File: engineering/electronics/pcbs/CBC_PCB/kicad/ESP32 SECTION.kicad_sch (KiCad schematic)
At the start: 20 parts, among them U2 2.4GHz, U4 1kΩ

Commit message: electronics: integrate CBC PCB updates
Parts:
- removed U4: 1kΩ, EasyEDA_Lib:R0402, symbol EasyEDA_Lib:MCS0402MC1001FE000
- added R69: 39Ω, EasyEDA_Lib:R0603, symbol CBC_PCB:0603WAF390JT5E
- C1: symbol EasyEDA_Lib:HGC0402R5105K250NTEJ -> CBC_PCB:HGC0402R5105K250NTEJ
- C18: symbol EasyEDA_Lib:CL21A475KBQNNNE -> CBC_PCB:CL21A475KBQNNNE
- C19, C22, C24: symbol EasyEDA_Lib:GRM21BR61H106KE43L -> CBC_PCB:GRM21BR61H106KE43L
- C20, C21, C23: symbol EasyEDA_Lib:CC0402KRX7R7BB104 -> CBC_PCB:CC0402KRX7R7BB104
- D3: symbol EasyEDA_Lib:SS14_C7420316 -> CBC_PCB:SS14_C7420316
- D4: symbol EasyEDA_Lib:USBLC6-2SC6 -> CBC_PCB:USBLC6-2SC6
- LED1: symbol EasyEDA_Lib:0603 Green 509-620mcd -> CBC_PCB:0603 Green 509-620mcd
- Q1: symbol EasyEDA_Lib:UMH3N -> CBC_PCB:UMH3N
- R7: symbol EasyEDA_Lib:RT0402BRD0710KL -> CBC_PCB:RT0402BRD0710KL
- R8, R9: symbol EasyEDA_Lib:0402WGF5101TCE -> CBC_PCB:0402WGF5101TCE
- SW1: symbol EasyEDA_Lib:TS-1088-AR02016 -> CBC_PCB:TS-1088-AR02016
- U2: symbol EasyEDA_Lib:ESP32-S3-WROOM-1(N16R8) -> CBC_PCB:ESP32-S3-WROOM-1(N16R8)
- U7: symbol EasyEDA_Lib:CP2104-F03-GM -> CBC_PCB:CP2104-F03-GM
- USB1: symbol EasyEDA_Lib:TYPE-C 16PIN 2MD(073) -> CBC_PCB:TYPE-C 16PIN 2MD(073)
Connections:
- net +3V3: now also R69.2
- net at LED1.2 (A): now also R69.1

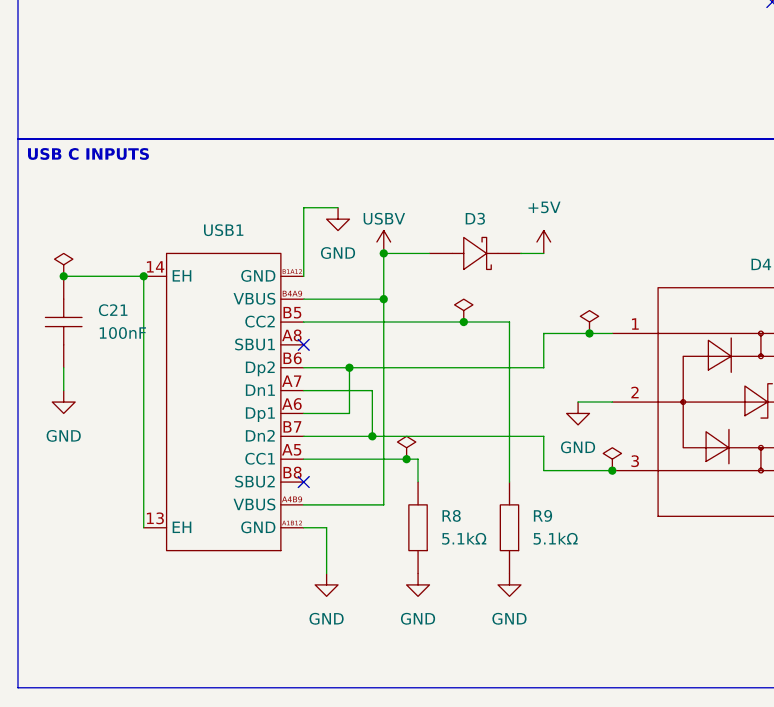
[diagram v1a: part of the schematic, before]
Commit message: pcb: update CBC import and routing rules
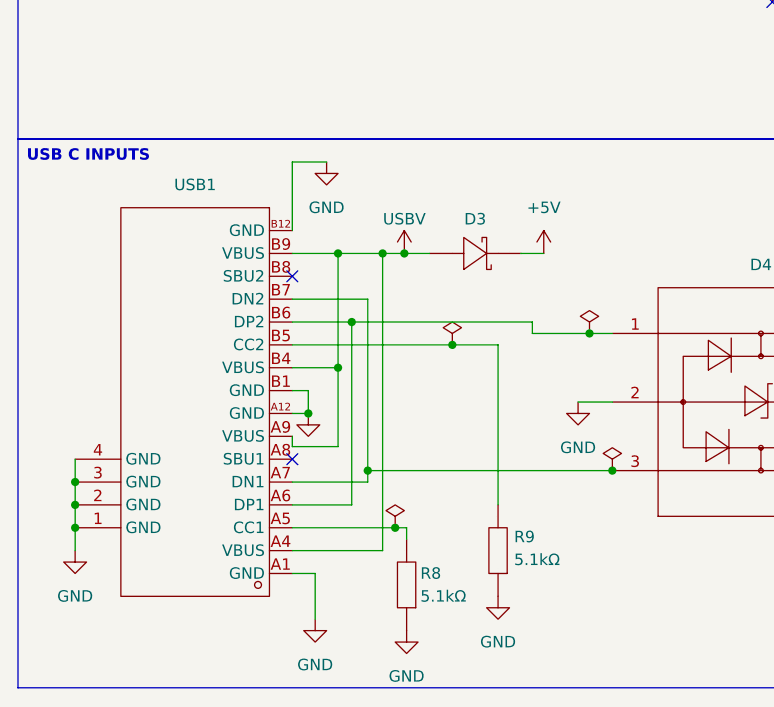
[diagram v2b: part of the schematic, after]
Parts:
- removed C21: 100nF, EasyEDA_Lib:C0402, symbol CBC_PCB:CC0402KRX7R7BB104
- USB1: footprint EasyEDA_Lib:USB-C-SMD_TYPE-C-16PIN-2MD-073 -> EasyEDA_Lib_2:USB-C-SMD_TYPEC-303-ACP16; symbol CBC_PCB:TYPE-C 16PIN 2MD(073) -> EasyEDA_Lib_2:TYPEC-303-ACP16; LCSC Part Name Type-C 母 卧贴 -> Type-C 母 立贴; Manufacturer SHOU HAN(首韩) -> XUNPU(讯普); Manufacturer Part TYPE-C 16PIN 2MD(073) -> TYPEC-303-ACP16; Supplier Part C2765186 -> C720628
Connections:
- net GND: now also USB1.1 (GND), USB1.2 (GND), USB1.3 (GND), USB1.4 (GND), USB1.A1 (GND), USB1.A12 (GND), USB1.B1 (GND), USB1.B12 (GND); no longer USB1.A1B12 (GND), USB1.B1A12 (GND)
- net USBV: now also USB1.A4 (VBUS), USB1.A9 (VBUS), USB1.B4 (VBUS), USB1.B9 (VBUS); no longer USB1.A4B9 (VBUS), USB1.B4A9 (VBUS)
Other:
- moved on the sheet: R8, R9
